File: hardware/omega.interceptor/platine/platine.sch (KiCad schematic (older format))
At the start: 15 parts, among them J1 USB_B_Micro, J3 RJ45, J4 RJ45, SW1 SW_DIP_x03, SW2 SW_DIP_x03, U1 LD1117S33TR_SOT223, U2 Omega2+

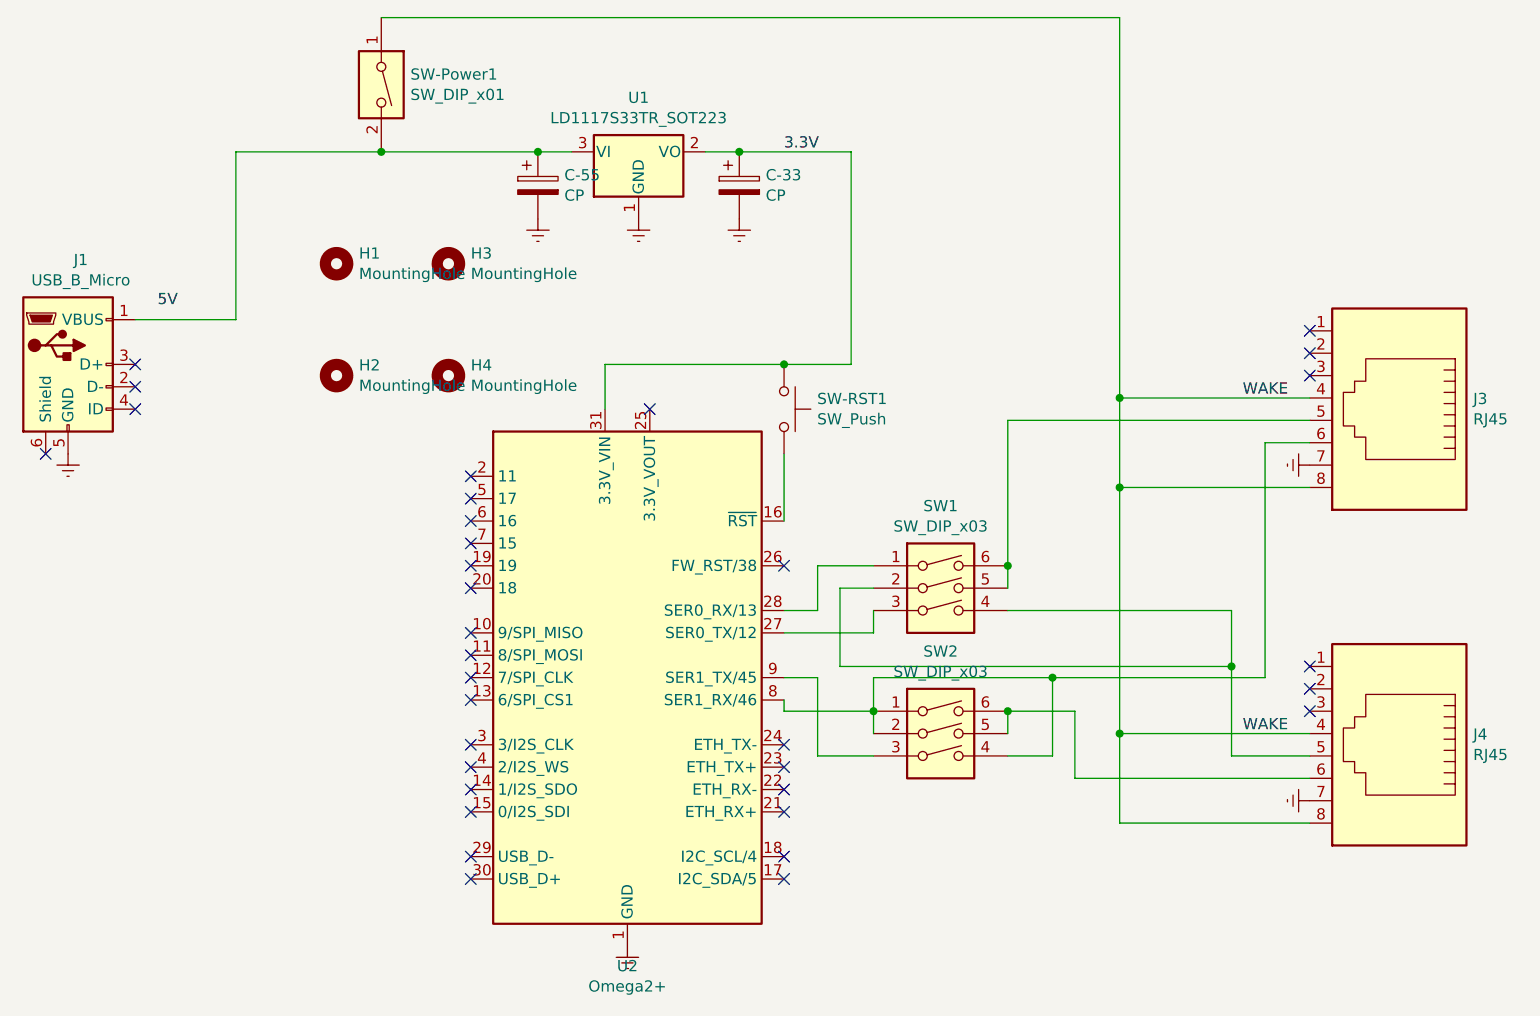
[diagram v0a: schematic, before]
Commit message: Signifikant changes to interceptor hardware layout * removed usb connector * removed switches for interceptor
made an easy setup to get it manifactured fast and to start testing the protocol
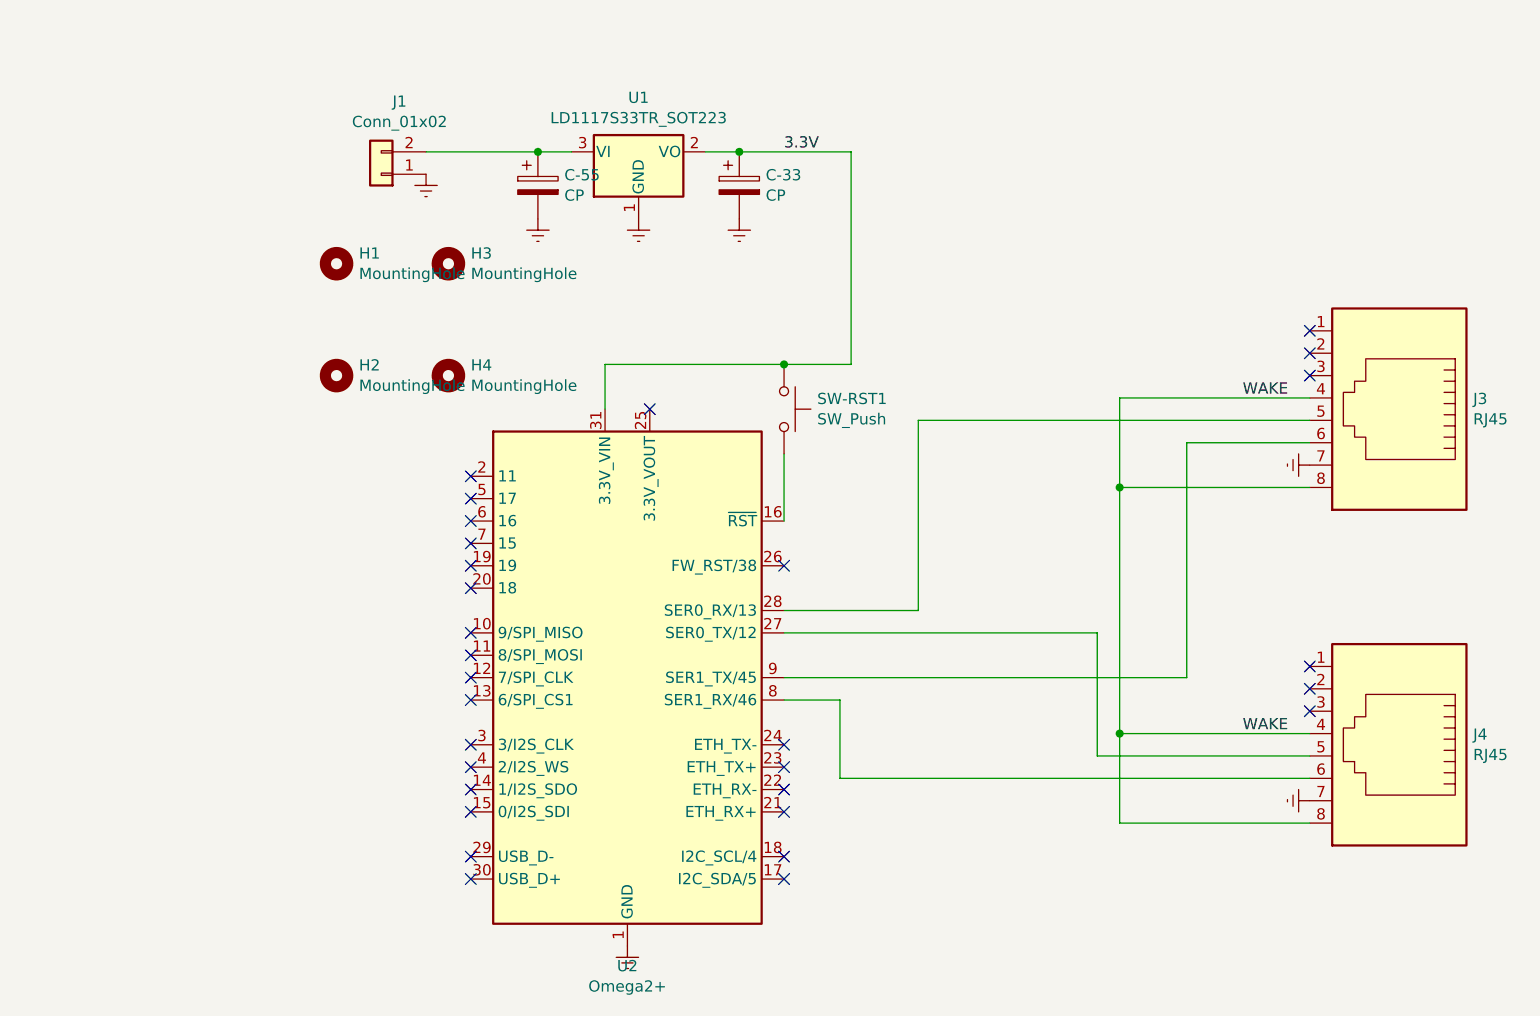
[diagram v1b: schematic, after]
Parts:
- removed J1: USB_B_Micro, Connector_USB:USB_Micro-AB_Molex_47590-0001, symbol Connector:USB_B_Micro
- removed SW-Power1: SW_DIP_x01, Button_Switch_THT:SW_DIP_SPSTx01_Slide_6.7x4.1mm_W7.62mm_P2.54mm_LowProfile, symbol Switch:SW_DIP_x01
- removed SW1, SW2: SW_DIP_x03, Button_Switch_THT:SW_DIP_SPSTx03_Slide_6.7x9.18mm_W7.62mm_P2.54mm_LowProfile, symbol Switch:SW_DIP_x03
- added J1: Conn_01x02, Connector_PinHeader_2.54mm:PinHeader_1x02_P2.54mm_Vertical, symbol Connector_Generic:Conn_01x02
- U2: footprint Module:Onion_Omega2+ -> Custom-Connectors:ONION_OMEGA2
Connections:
- net Earth: now also J1.1 (Pin_1)
- net at C-55.1, U1.3 (VI): now also J1.2 (Pin_2)
- net at J3.5: now also U2.28 (SER0_RX/13)
- net at J3.6: now also U2.9 (SER1_TX/45); no longer U2.8 (SER1_RX/46)
- net at J4.5: now also U2.27 (SER0_TX/12)
- net at J4.6: now also U2.8 (SER1_RX/46)
- no-connect marks 34 -> 30
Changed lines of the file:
@@
 	6750 1300 7250 1300
 Connection ~ 6750 1300
-Connection ~ 5850 1300
 NoConn ~ 9300 2100
 NoConn ~ 9300 2200
@@
 Wire Wire Line
 	9300 2400 8450 2400
-Connection ~ 8450 2400
 Wire Wire Line
 	9300 3900 8450 3900
@@
 Wire Wire Line
 	8450 3900 8450 4300
-Text Label 4150 2000 0    50   ~ 0
-5V
 Text Label 6950 1300 0    50   ~ 0
 3.3V
@@
 Text Label 9000 3900 0    50   ~ 0
 WAKE
-Wire Wire Line
-	4500 1300 5150 1300
-$Comp
-L Switch:SW_DIP_x01 SW-Power1
-U 1 1 5E954C19
-P 5150 1000
-F 0 "SW-Power1" V 5104 1130 50  0000 L CNN
-F 1 "SW_DIP_x01" V 5195 1130 50  0000 L CNN
-F 2 "Button_Switch_THT:SW_DIP_SPSTx01_Slide_6.7x4.1mm_W7.62mm_P2.54mm_LowProfile" H 5150 1000 50  0001 C CNN
-F 3 "~" H 5150 1000 50  0001 C CNN
-	1    5150 1000
-	0    1    1    0
-$EndComp
-Connection ~ 5150 1300
-Wire Wire Line
-	5150 1300 5850 1300
-Wire Wire Line
-	5150 700  8450 700
-Wire Wire Line
-	8450 700  8450 2400
 $Comp
 L power:Earth #PWR0101
@@
 $EndComp
 $Comp
-L Connector:USB_B_Micro J1
-U 1 1 5E850005
-P 3750 2250
-F 0 "J1" H 3807 2717 50  0000 C CNN
-F 1 "USB_B_Micro" H 3807 2626 50  0000 C CNN
-F 2 "Connector_USB:USB_Micro-AB_Molex_47590-0001" H 3900 2200 50  0001 C CNN
-F 3 "~" H 3900 2200 50  0001 C CNN
-	1    3750 2250
-	1    0    0    -1
-$EndComp
-Wire Wire Line
-	4050 2050 4500 2050
-Wire Wire Line
-	4500 1300 4500 2050
-NoConn ~ 4050 2250
-NoConn ~ 4050 2350
-NoConn ~ 4050 2450
-$Comp
-L power:Earth #PWR0107
-U 1 1 5E85EFD1
-P 3750 2650
-F 0 "#PWR0107" H 3750 2400 50  0001 C CNN
-F 1 "Earth" H 3750 2500 50  0001 C CNN
-F 2 "" H 3750 2650 50  0001 C CNN
-F 3 "~" H 3750 2650 50  0001 C CNN
-	1    3750 2650
-	1    0    0    -1
-$EndComp
-NoConn ~ 3650 2650
-$Comp
-L MCU_Module:Omega2+ U2
-U 1 1 5E976E24
-P 6250 3650
-F 0 "U2" H 6250 2361 50  0000 C CNN
-F 1 "Omega2+" H 6250 2270 50  0000 C CNN
-F 2 "Module:Onion_Omega2+" H 6250 2150 50  0001 C CNN
-F 3 "https://docs.onion.io/omega2-docs/omega2p.html" H 3050 2500 50  0001 C CNN
-	1    6250 3650
-	1    0    0    -1
-$EndComp
-$Comp
-L Switch:SW_DIP_x03 SW1
-U 1 1 5E881767
-P 7650 3350
-F 0 "SW1" H 7650 3817 50  0000 C CNN
-F 1 "SW_DIP_x03" H 7650 3726 50  0000 C CNN
-F 2 "Button_Switch_THT:SW_DIP_SPSTx03_Slide_6.7x9.18mm_W7.62mm_P2.54mm_LowProfile" H 7650 3350 50  0001 C CNN
-F 3 "~" H 7650 3350 50  0001 C CNN
-	1    7650 3350
-	1    0    0    -1
-$EndComp
-$Comp
-L Switch:SW_DIP_x03 SW2
-U 1 1 5E8820C7
-P 7650 4000
-F 0 "SW2" H 7650 4467 50  0000 C CNN
-F 1 "SW_DIP_x03" H 7650 4376 50  0000 C CNN
-F 2 "Button_Switch_THT:SW_DIP_SPSTx03_Slide_6.7x9.18mm_W7.62mm_P2.54mm_LowProfile" H 7650 4000 50  0001 C CNN
-F 3 "~" H 7650 4000 50  0001 C CNN
-	1    7650 4000
-	1    0    0    -1
-$EndComp
-Wire Wire Line
-	9300 2500 7950 2500
-Wire Wire Line
-	7950 2500 7950 3150
-Wire Wire Line
-	7350 3150 7100 3150
-Wire Wire Line
-	7100 3150 7100 3350
-Wire Wire Line
-	7100 3350 6950 3350
-Wire Wire Line
-	7950 3150 7950 3250
-Connection ~ 7950 3150
-Wire Wire Line
-	6950 3450 7350 3450
-Wire Wire Line
-	7350 3450 7350 3350
-Wire Wire Line
-	7350 3250 7200 3250
-Wire Wire Line
-	7200 3250 7200 3600
-Wire Wire Line
-	7200 3600 8950 3600
-Wire Wire Line
-	8950 3600 8950 4000
-Wire Wire Line
-	8950 4000 9300 4000
-Wire Wire Line
-	7950 3350 8950 3350
-Wire Wire Line
-	8950 3350 8950 3600
-Connection ~ 8950 3600
-Wire Wire Line
-	9300 4100 8250 4100
-Wire Wire Line
-	8250 4100 8250 3800
-Wire Wire Line
-	8250 3800 7950 3800
-Wire Wire Line
-	7350 3800 6950 3800
-Wire Wire Line
-	6950 3800 6950 3750
-Wire Wire Line
-	7950 3800 7950 3900
-Connection ~ 7950 3800
-Wire Wire Line
-	6950 3650 7100 3650
-Wire Wire Line
-	7100 3650 7100 4000
-Wire Wire Line
-	7100 4000 7350 4000
-Wire Wire Line
-	7350 3900 7350 3800
-Wire Wire Line
-	7350 3650 8150 3650
-Wire Wire Line
-	9100 3650 9100 2600
-Wire Wire Line
-	9100 2600 9300 2600
-Connection ~ 7350 3800
-Wire Wire Line
-	7350 3800 7350 3650
-Wire Wire Line
-	7950 4000 8150 4000
-Wire Wire Line
-	8150 4000 8150 3650
-Connection ~ 8150 3650
-Wire Wire Line
-	8150 3650 9100 3650
-$Comp
 L Mechanical:MountingHole H1
 U 1 1 5E8B58E2
@@
 	1    0    0    -1
 $EndComp
+$Comp
+L MCU_Module:Omega2+ U2
+U 1 1 5E976E24
+P 6250 3650
+F 0 "U2" H 6250 2361 50  0000 C CNN
+F 1 "Omega2+" H 6250 2270 50  0000 C CNN
+F 2 "Custom-Connectors:ONION_OMEGA2" H 6250 2150 50  0001 C CNN
+F 3 "https://docs.onion.io/omega2-docs/omega2p.html" H 3050 2500 50  0001 C CNN
+	1    6250 3650
+	1    0    0    -1
+$EndComp
+Wire Wire Line
+	9300 2500 7550 2500
+Wire Wire Line
+	7550 2500 7550 3350
+Wire Wire Line
+	7550 3350 6950 3350
+Wire Wire Line
+	6950 3450 8350 3450
+Wire Wire Line
+	8350 3450 8350 4000
+Wire Wire Line
+	8350 4000 9300 4000
+Wire Wire Line
+	9300 4100 7200 4100
+Wire Wire Line
+	7200 4100 7200 3750
+Wire Wire Line
+	7200 3750 6950 3750
+Wire Wire Line
+	6950 3650 8750 3650
+Wire Wire Line
+	8750 3650 8750 2600
+Wire Wire Line
+	8750 2600 9300 2600
+$Comp
+L Connector_Generic:Conn_01x02 J1
+U 1 1 5EF3C7D3
+P 5150 1400
+F 0 "J1" H 5068 1075 50  0000 C CNN
+F 1 "Conn_01x02" H 5068 1166 50  0000 C CNN
+F 2 "Connector_PinHeader_2.54mm:PinHeader_1x02_P2.54mm_Vertical" H 5150 1400 50  0001 C CNN
+F 3 "~" H 5150 1400 50  0001 C CNN
+	1    5150 1400
+	-1   0    0    1
+$EndComp
+Wire Wire Line
+	5350 1300 5850 1300
+Connection ~ 5850 1300
+$Comp
+L power:Earth #PWR0107
+U 1 1 5EF4874D
+P 5350 1400
+F 0 "#PWR0107" H 5350 1150 50  0001 C CNN
+F 1 "Earth" H 5350 1250 50  0001 C CNN
+F 2 "" H 5350 1400 50  0001 C CNN
+F 3 "~" H 5350 1400 50  0001 C CNN
+	1    5350 1400
+	1    0    0    -1
+$EndComp
